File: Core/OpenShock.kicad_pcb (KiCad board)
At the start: 2 copper layers, 49.2 x 75.7 mm, 83 parts, among them CN1 PJ-3200-3A, J1 USB_C_Receptacle_USB2.0, J2 Conn_01x03_Socket, J3 Conn_01x03_Socket, J4 Conn_01x07_Socket, J6 USB Breakout, SW1 SW_SPST, SW2 SW_SPST, SW3 SW_SPST, U1 ESP32-S3-WROOM-1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

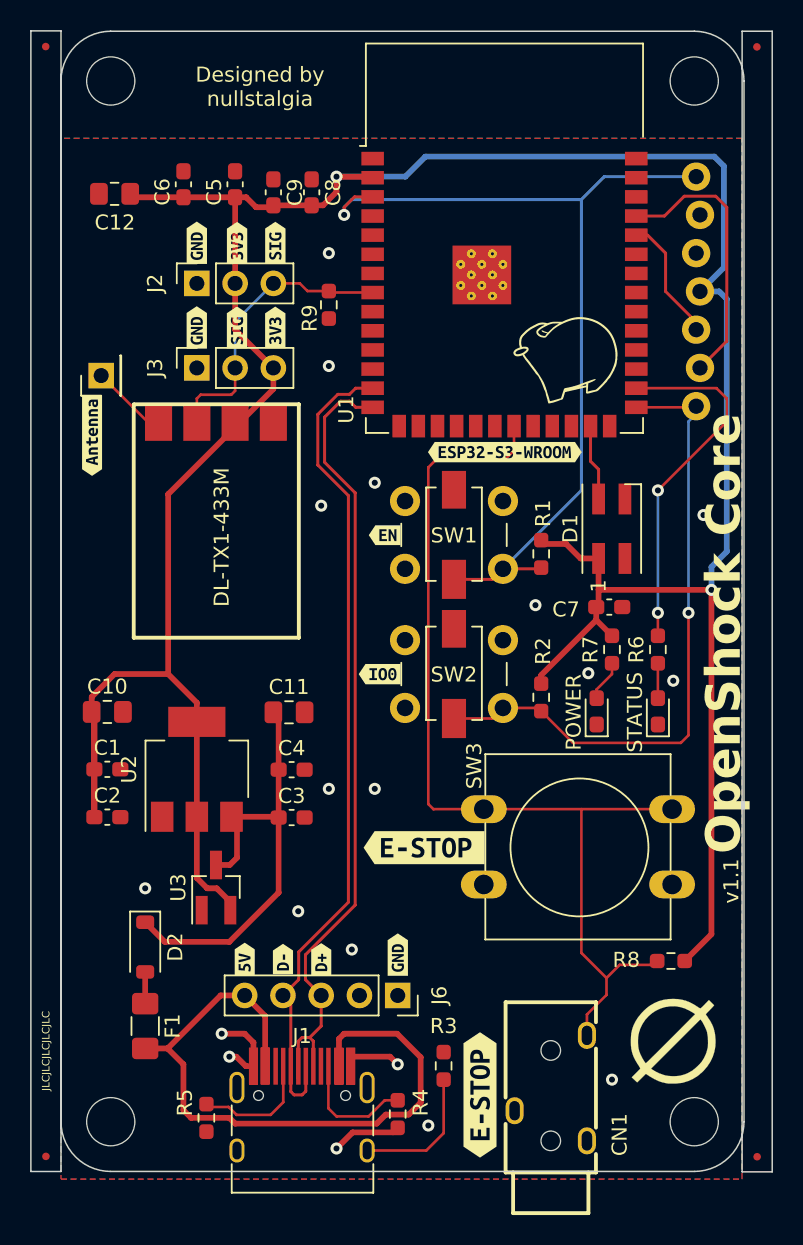
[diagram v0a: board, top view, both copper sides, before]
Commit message: OpenShock Core V1.2, fixes dumb short between 3v3 and GND
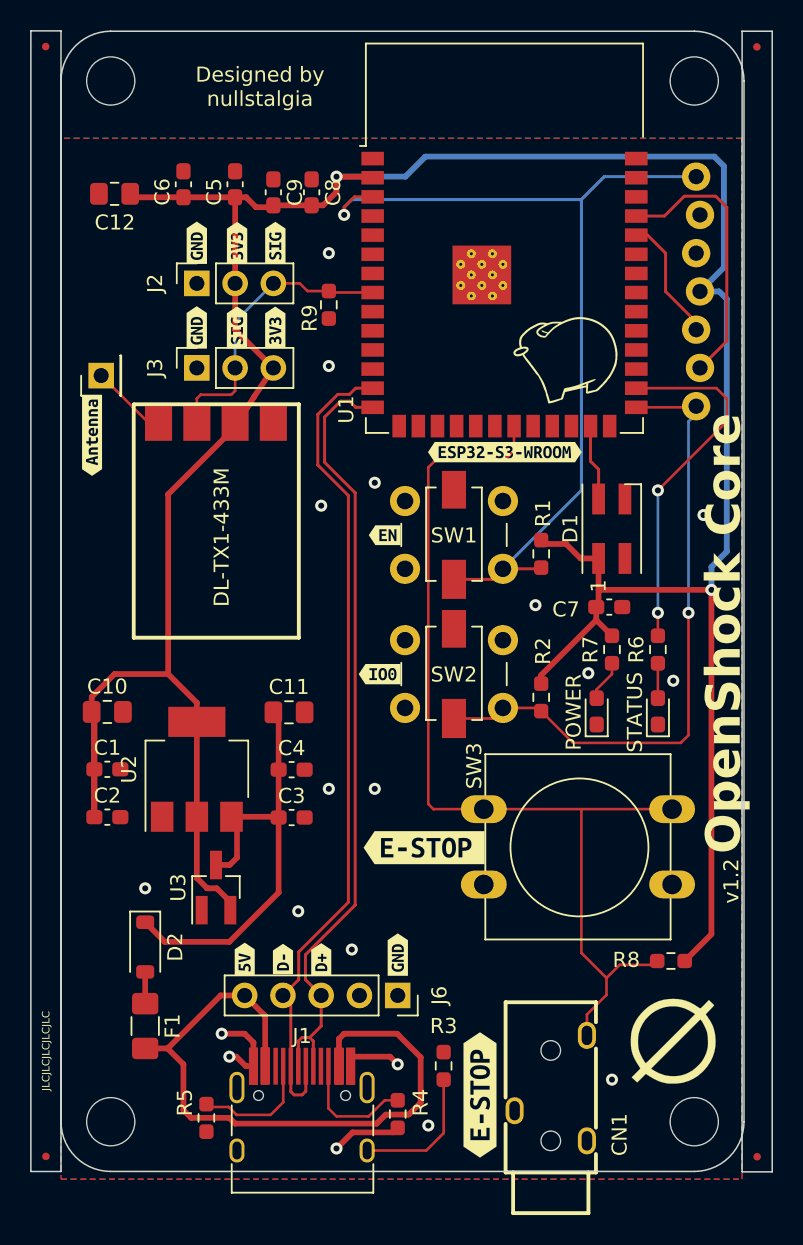
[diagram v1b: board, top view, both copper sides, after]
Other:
- board text added: "v1.2"
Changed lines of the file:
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@@
     (property "ki_description" "Generic connector, single row, 01x05, script generated")
     (property "ki_keywords" "connector")
-    (attr through_hole exclude_from_pos_files)
+    (attr through_hole exclude_from_pos_files exclude_from_bom)
     (fp_text reference "J6" (at 0 -2.77 90) (layer "F.SilkS")
         (effects (font (size 1 1) (thickness 0.15)))
@@
     (property "Sheetfile" "USBMuxBreakout.kicad_sch")
     (property "Sheetname" "")
-    (attr smd)
+    (attr smd exclude_from_pos_files exclude_from_bom)
     (fp_text reference "FID4" (at 0 -1.5 90) (layer "F.Fab")
         (effects (font (size 1 1) (thickness 0.15)))
@@
     (property "Sheetfile" "USBMuxBreakout.kicad_sch")
     (property "Sheetname" "")
-    (attr smd)
+    (attr smd exclude_from_pos_files exclude_from_bom)
     (fp_text reference "FID1" (at 0 -1.5 90) (layer "F.Fab")
         (effects (font (size 1 1) (thickness 0.15)))
@@
     (property "ki_description" "Generic connector, single row, 01x03, script generated")
     (property "ki_keywords" "connector")
-    (attr through_hole exclude_from_pos_files)
+    (attr through_hole exclude_from_pos_files exclude_from_bom)
     (fp_text reference "J3" (at 0 -2.77 90) (layer "F.SilkS")
         (effects (font (size 1 1) (thickness 0.15)))
@@
     (property "ki_description" "Single Pole Single Throw (SPST) switch")
     (property "ki_keywords" "switch lever")
-    (attr through_hole exclude_from_pos_files)
+    (attr through_hole exclude_from_pos_files exclude_from_bom)
     (fp_text reference "SW3" (at -0.635 -2.874 90) (layer "F.SilkS")
         (effects (font (size 1 1) (thickness 0.15)))
@@
     (property "ki_description" "250mA Low Quiscent Current LDO, 3.0V output, SOT-23")
     (property "ki_keywords" "regulator linear ldo")
-    (attr smd exclude_from_pos_files)
+    (attr smd exclude_from_pos_files exclude_from_bom)
     (fp_text reference "U3" (at 0 -2.5 90) (layer "F.SilkS")
         (effects (font (size 1 1) (thickness 0.15)))
@@
     (property "ki_description" "Generic connector, single row, 01x03, script generated")
     (property "ki_keywords" "connector")
-    (attr through_hole exclude_from_pos_files)
+    (attr through_hole exclude_from_pos_files exclude_from_bom)
     (fp_text reference "J2" (at 0 -2.77 90) (layer "F.SilkS")
         (effects (font (size 1 1) (thickness 0.15)))
@@
     (property "ki_description" "Generic connector, single row, 01x07, script generated")
     (property "ki_keywords" "connector")
-    (attr exclude_from_pos_files)
+    (attr exclude_from_pos_files exclude_from_bom)
     (fp_text reference "J4" (at 0 1.905 90) (layer "B.Fab")
         (effects (font (size 0.6096 0.6096) (thickness 0.127)) (justify mirror))
@@
     )
   )
-  (gr_text "v1.1" (at 144.653 93.98 90) (layer "F.SilkS")
+  (gr_text "v1.2" (at 144.653 93.98 90) (layer "F.SilkS")
     (effects (font (size 1 1) (thickness 0.15)) (justify left bottom))
   )
@@
   (segment (start 108.585 80.645) (end 108.585 81.915) (width 0.381) (layer "F.Cu") (net 1))
   (segment (start 106.68 78.74) (end 108.585 80.645) (width 0.381) (layer "F.Cu") (net 1))
+  (segment (start 112.395 60.325) (end 111.125 62.357) (width 0.381) (layer "F.Cu") (net 1))
   (segment (start 131.445 78.811) (end 131.445 79.375) (width 0.381) (layer "F.Cu") (net 1))
   (segment (start 133.096 70.104) (end 131.699 70.104) (width 0.381) (layer "F.Cu") (net 1))
-  (segment (start 113.665 59.817) (end 111.125 62.357) (width 0.381) (layer "F.Cu") (net 1))
   (segment (start 135.1 74.295) (end 135.1 75.156) (width 0.381) (layer "F.Cu") (net 1))
   (segment (start 111.8605 47.0905) (end 112.522 47.752) (width 0.381) (layer "F.Cu") (net 1))
@@
   (segment (start 113.538 47.752) (end 113.665 47.625) (width 0.381) (layer "F.Cu") (net 1))
   (segment (start 120.181 45.72) (end 117.856 45.72) (width 0.381) (layer "F.Cu") (net 1))
+  (segment (start 106.68 66.802) (end 106.68 78.74) (width 0.381) (layer "F.Cu") (net 1))
   (segment (start 117.856 45.72) (end 117.856 46.736) (width 0.381) (layer "F.Cu") (net 1))
-  (segment (start 111.125 62.357) (end 106.68 66.802) (width 0.381) (layer "F.Cu") (net 1))
   (segment (start 101.605 81.255) (end 101.605 80.259) (width 0.381) (layer "F.Cu") (net 1))
   (segment (start 108.585 81.915) (end 108.585 88.215) (width 0.381) (layer "F.Cu") (net 1))
@@
   (segment (start 117.856 46.736) (end 116.967 47.625) (width 0.381) (layer "F.Cu") (net 1))
   (segment (start 142.748 73.152) (end 142.748 96.012) (width 0.381) (layer "F.Cu") (net 1))
-  (segment (start 106.68 66.802) (end 106.68 78.74) (width 0.381) (layer "F.Cu") (net 1))
   (segment (start 111.125 55.88) (end 113.665 58.42) (width 0.381) (layer "F.Cu") (net 1))
   (segment (start 101.78 88.24) (end 101.78 85.065) (width 0.381) (layer "F.Cu") (net 1))
   (segment (start 116.205 47.625) (end 113.665 47.625) (width 0.381) (layer "F.Cu") (net 1))
+  (segment (start 113.665 58.42) (end 112.395 60.325) (width 0.381) (layer "F.Cu") (net 1))
   (segment (start 108.585 92.276) (end 108.585 88.215) (width 0.381) (layer "F.Cu") (net 1))
   (segment (start 104.389 47.0905) (end 104.1615 46.863) (width 0.381) (layer "F.Cu") (net 1))
+  (segment (start 111.125 62.357) (end 106.68 66.802) (width 0.381) (layer "F.Cu") (net 1))
   (segment (start 131.699 70.104) (end 131.445 69.85) (width 0.381) (layer "F.Cu") (net 1))
   (segment (start 101.78 81.43) (end 101.78 88.24) (width 0.381) (layer "F.Cu") (net 1))
   (segment (start 103.124 78.74) (end 106.68 78.74) (width 0.381) (layer "F.Cu") (net 1))
-  (segment (start 113.665 58.42) (end 113.665 59.817) (width 0.381) (layer "F.Cu") (net 1))
   (segment (start 135.255 71.067) (end 134.059 71.067) (width 0.381) (layer "F.Cu") (net 1))
   (segment (start 110.805 94.415) (end 110.805 93.865) (width 0.381) (layer "F.Cu") (net 1))
